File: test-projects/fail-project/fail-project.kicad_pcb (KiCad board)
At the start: 2 copper layers, 14 x 9 mm, 3 parts, among them J1 Conn_01x02

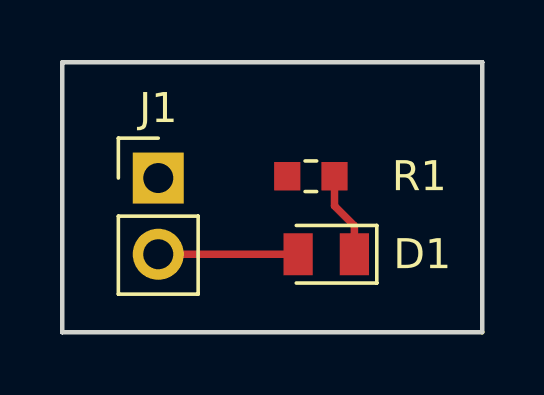
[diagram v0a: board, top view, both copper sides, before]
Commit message: Add UI automation for PCBNew DRC
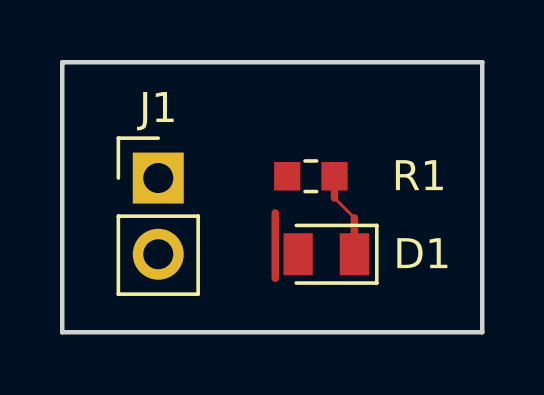
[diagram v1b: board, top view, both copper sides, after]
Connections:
- R1 pad 2: GND -> (no net)
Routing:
- net VCC: track 4.66 -> 0.00 mm
- net (no net): track 0.00 -> 2.17 mm
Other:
- board text added: "The track between R1 and D1 contains a section with a width that is too small There is a random trace that is too close to pad 2 of D1 We expect to see 2 DRC errors"
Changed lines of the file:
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@@
 (kicad_pcb (version 4) (host pcbnew 4.0.7)
   (general
-    (links 3)
-    (no_connects 0)
+    (links 2)
+    (no_connects 1)
     (area 138.924999 101.924999 153.075001 111.075001)
     (thickness 1.6)
-    (drawings 4)
+    (drawings 5)
     (tracks 4)
     (zones 0)
@@
     (pad 1 smd rect (at -0.7875 0 180) (size 0.875 0.95) (layers F.Cu F.Paste F.Mask)
       (net 1 "Net-(D1-Pad1)"))
-    (pad 2 smd rect (at 0.7875 0 180) (size 0.875 0.95) (layers F.Cu F.Paste F.Mask)
-      (net 3 GND))
+    (pad 2 smd rect (at 0.7875 0 180) (size 0.875 0.95) (layers F.Cu F.Paste F.Mask))
     (model ${KISYS3DMOD}/Resistor_SMD.3dshapes/R_0603_1608Metric.wrl
       (at (xyz 0 0 0))
@@
     )
   )
+  (gr_text "The track between R1 and D1 contains a section with a width that is too small\nThere is a random trace that is too close to pad 2 of D1\nWe expect to see 2 DRC errors" (at 146.6 112.4) (layer Dwgs.User)
+    (effects (font (size 0.5 0.5) (thickness 0.1)))
+  )
   (gr_line (start 139 111) (end 139 102) (layer Edge.Cuts) (width 0.15))
   (gr_line (start 153 111) (end 139 111) (layer Edge.Cuts) (width 0.15))
   (gr_line (start 153 102) (end 153 111) (layer Edge.Cuts) (width 0.15))
   (gr_line (start 139 102) (end 153 102) (layer Edge.Cuts) (width 0.15))
-  (segment (start 148.7375 108.4) (end 148.7375 107.45) (width 0.25) (layer F.Cu) (net 1))
-  (segment (start 148.7375 107.45) (end 148.075 106.7875) (width 0.25) (layer F.Cu) (net 1))
-  (segment (start 148.075 106.7875) (end 148.075 105.8) (width 0.25) (layer F.Cu) (net 1))
-  (segment (start 142.2 108.4) (end 146.8625 108.4) (width 0.25) (layer F.Cu) (net 2))
+  (segment (start 146.1 107.025) (end 146.1 109.2) (width 0.25) (layer F.Cu) (net 0))
+  (segment (start 148.075 106.525) (end 148.7375 107.1875) (width 0.1) (layer F.Cu) (net 1))
+  (segment (start 148.075 105.8) (end 148.075 106.525) (width 0.25) (layer F.Cu) (net 1))
+  (segment (start 148.7375 107.1875) (end 148.7375 108.4) (width 0.25) (layer F.Cu) (net 1))
   (zone (net 3) (net_name GND) (layer F.Cu) (hatch edge 0.508)
     (connect_pads (clearance 0.508))

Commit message: Update test projects to KiCad 5
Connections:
- R1 pad 2: (no net) -> Net-(R1-Pad2)
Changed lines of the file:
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@@
-(kicad_pcb (version 4) (host pcbnew 4.0.7)
+(kicad_pcb (version 20171130) (host pcbnew 5.0.1-33cea8e~67~ubuntu18.04.1)
   (general
-    (links 2)
-    (no_connects 1)
-    (area 138.924999 101.924999 153.075001 111.075001)
     (thickness 1.6)
     (drawings 5)
@@
     (zones 0)
     (modules 3)
-    (nets 4)
+    (nets 5)
   )
   (page A4)
@@
     (pad_drill 0.762)
     (pad_to_mask_clearance 0.2)
+    (solder_mask_min_width 0.25)
     (aux_axis_origin 0 0)
     (visible_elements FFFFFF7F)
@@
       (layerselection 0x00030_80000001)
       (usegerberextensions false)
+      (usegerberattributes false)
+      (usegerberadvancedattributes false)
+      (creategerberjobfile false)
       (excludeedgelayer true)
       (linewidth 0.050000)
@@
       (hpglpennumber 1)
       (hpglpenspeed 20)
-      (hpglpendiameter 15)
-      (hpglpenoverlay 2)
+      (hpglpendiameter 15.000000)
       (psnegative false)
       (psa4output false)
@@
   (net 2 VCC)
   (net 3 GND)
+  (net 4 "Net-(R1-Pad2)")
   (net_class Default "This is the default net class."
     (clearance 0.2)
@@
     (add_net GND)
     (add_net "Net-(D1-Pad1)")
+    (add_net "Net-(R1-Pad2)")
     (add_net VCC)
   )
@@
     (pad 1 smd rect (at -0.7875 0 180) (size 0.875 0.95) (layers F.Cu F.Paste F.Mask)
       (net 1 "Net-(D1-Pad1)"))
-    (pad 2 smd rect (at 0.7875 0 180) (size 0.875 0.95) (layers F.Cu F.Paste F.Mask))
+    (pad 2 smd rect (at 0.7875 0 180) (size 0.875 0.95) (layers F.Cu F.Paste F.Mask)
+      (net 4 "Net-(R1-Pad2)"))
     (model ${KISYS3DMOD}/Resistor_SMD.3dshapes/R_0603_1608Metric.wrl
       (at (xyz 0 0 0))
